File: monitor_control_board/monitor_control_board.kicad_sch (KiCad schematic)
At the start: 21 parts, among them J1 Conn_01x09_Male, J2 Conn_01x09_Male, J3 Conn_01x05_Male, J4 Conn_01x05_Male, SW1 SW_Push, SW2 SW_Push, SW3 SW_Push, SW4 SW_Push, SW5 SW_Push, SW6 SW_Push, U1 TSSP58038

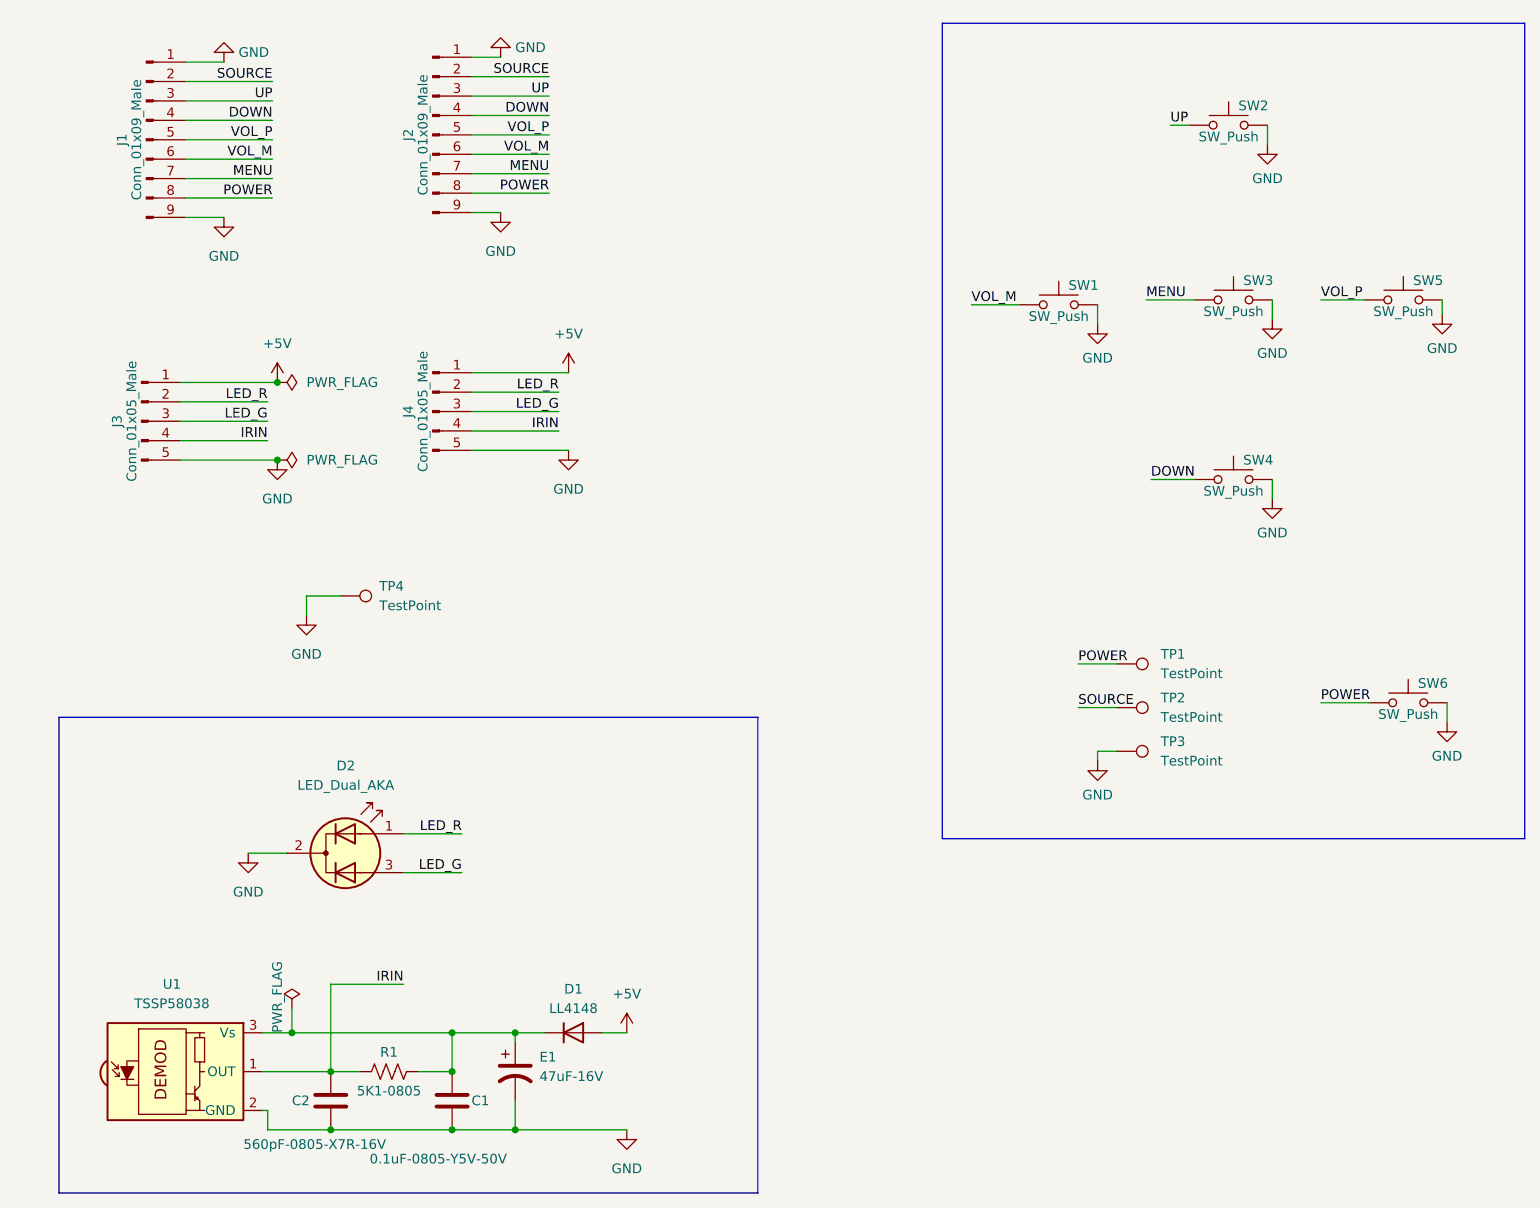
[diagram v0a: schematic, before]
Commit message: osd 컨트롤 보드 사소한 위치 조정
Signed-off-by: Ju, Gyeong-min <jcmh74@gmail.com>
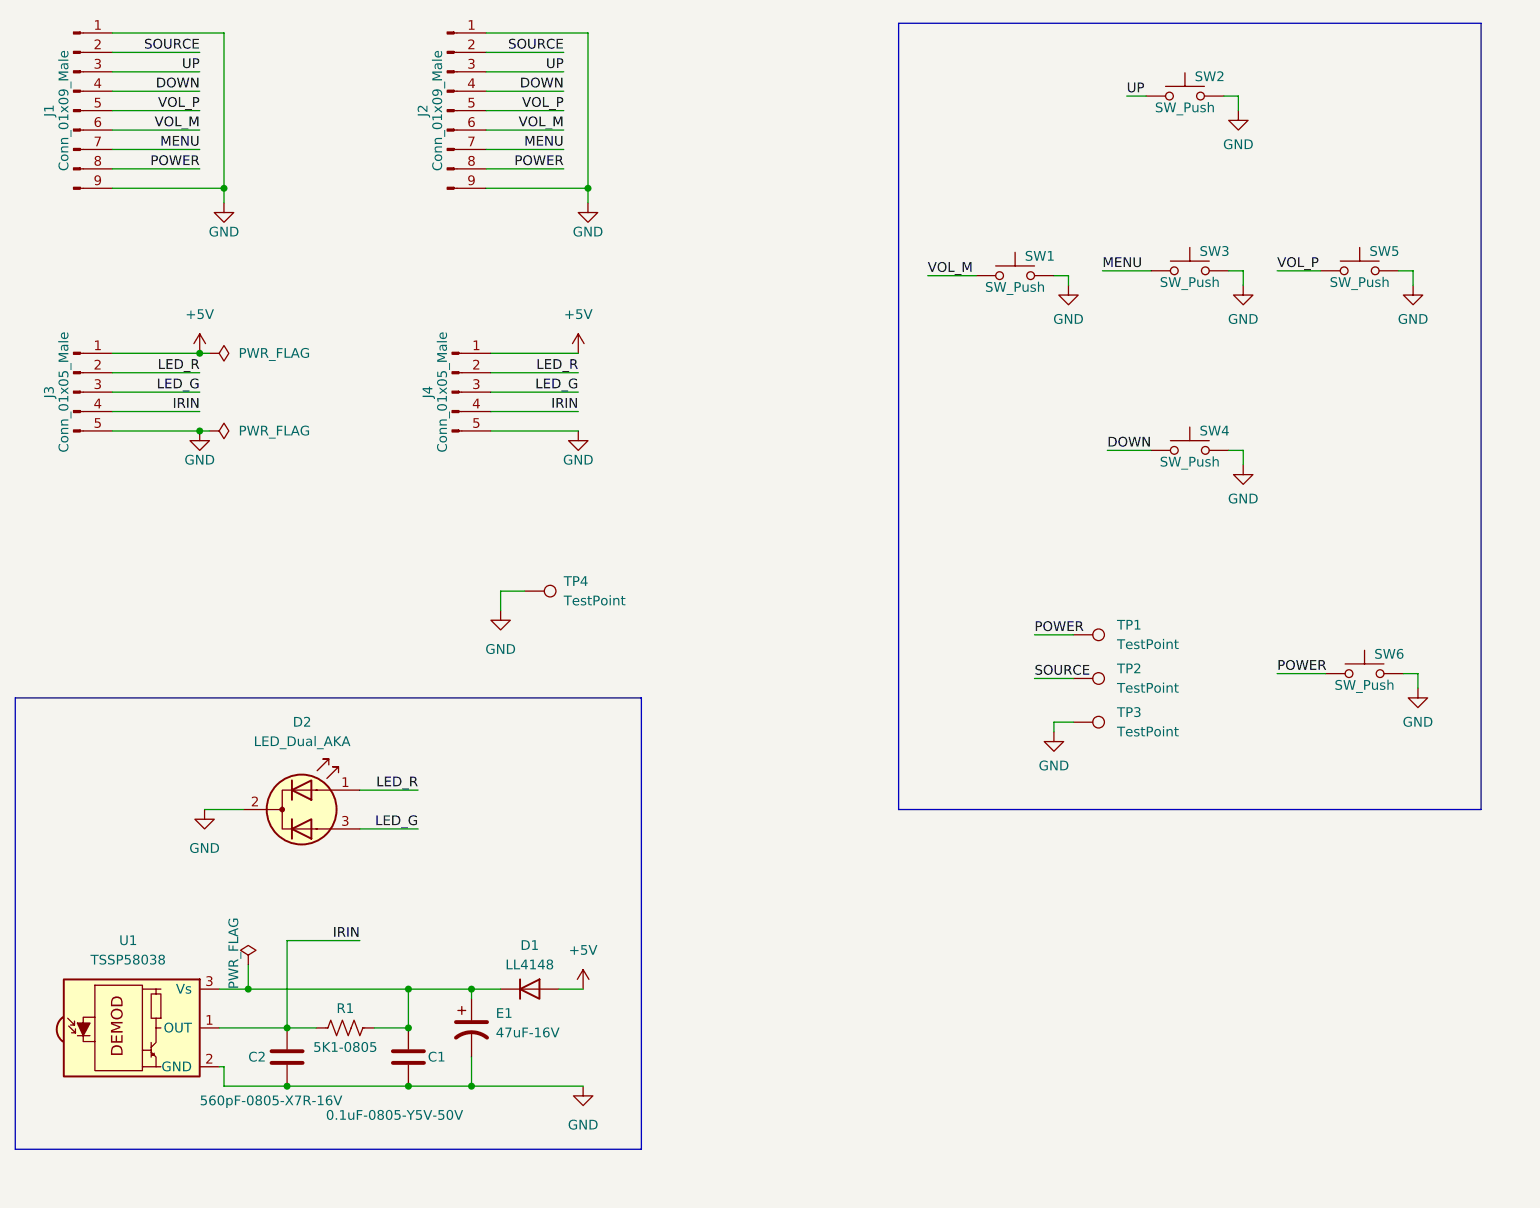
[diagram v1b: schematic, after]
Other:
- moved on the sheet: C1, C2, D1, D2, E1, J1, J2, J3, J4, R1, SW1, SW2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

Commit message: monitor_osd 배선 최적화
Signed-off-by: Ju, Gyeong-min <jcmh74@gmail.com>
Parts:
- TP1, TP2, TP3: footprint TestPoint:TestPoint_THTPad_D2.0mm_Drill1.0mm -> TestPoint:TestPoint_THTPad_D1.5mm_Drill0.7mm
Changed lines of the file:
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@@
       (effects (font (size 1.27 1.27)) (justify left))
     )
-    (property "Footprint" "TestPoint:TestPoint_THTPad_D2.0mm_Drill1.0mm" (id 2) (at 193.04 114.3 0)
+    (property "Footprint" "TestPoint:TestPoint_THTPad_D1.5mm_Drill0.7mm" (id 2) (at 193.04 114.3 0)
       (effects (font (size 1.27 1.27)) hide)
     )
@@
       (effects (font (size 1.27 1.27)) (justify left))
     )
-    (property "Footprint" "TestPoint:TestPoint_THTPad_D2.0mm_Drill1.0mm" (id 2) (at 193.04 120.015 0)
+    (property "Footprint" "TestPoint:TestPoint_THTPad_D1.5mm_Drill0.7mm" (id 2) (at 193.04 120.015 0)
       (effects (font (size 1.27 1.27)) hide)
     )
@@
       (effects (font (size 1.27 1.27)) (justify left))
     )
-    (property "Footprint" "TestPoint:TestPoint_THTPad_D2.0mm_Drill1.0mm" (id 2) (at 193.04 125.73 0)
+    (property "Footprint" "TestPoint:TestPoint_THTPad_D1.5mm_Drill0.7mm" (id 2) (at 193.04 125.73 0)
       (effects (font (size 1.27 1.27)) hide)
     )
@@
     )
     (path "/28135604-dc7c-4d8f-bee5-8abb6d80f68a"
-      (reference "TP1") (unit 1) (value "TestPoint") (footprint "TestPoint:TestPoint_THTPad_D2.0mm_Drill1.0mm")
+      (reference "TP1") (unit 1) (value "TestPoint") (footprint "TestPoint:TestPoint_THTPad_D1.5mm_Drill0.7mm")
     )
     (path "/3b934f31-2bae-48a3-8048-7da2c4d085a5"
-      (reference "TP2") (unit 1) (value "TestPoint") (footprint "TestPoint:TestPoint_THTPad_D2.0mm_Drill1.0mm")
+      (reference "TP2") (unit 1) (value "TestPoint") (footprint "TestPoint:TestPoint_THTPad_D1.5mm_Drill0.7mm")
     )
     (path "/c9f71dc3-2b4a-4ca2-8db0-36825f55689f"
-      (reference "TP3") (unit 1) (value "TestPoint") (footprint "TestPoint:TestPoint_THTPad_D2.0mm_Drill1.0mm")
+      (reference "TP3") (unit 1) (value "TestPoint") (footprint "TestPoint:TestPoint_THTPad_D1.5mm_Drill0.7mm")
     )
     (path "/a4e9f764-09ab-446a-a555-ce94ff4e73f7"

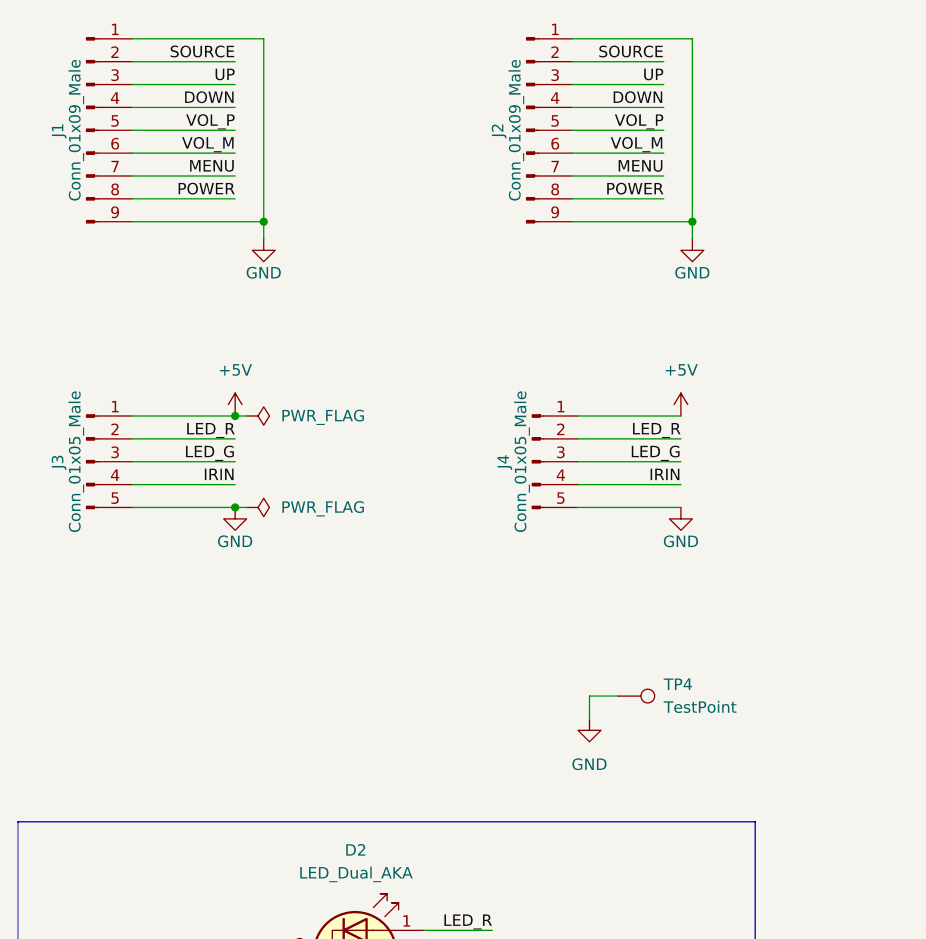
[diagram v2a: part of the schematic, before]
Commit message: monitor_osd 커넥터 모양 및 위치 변경
Signed-off-by: Ju, Gyeong-min <jcmh74@gmail.com>
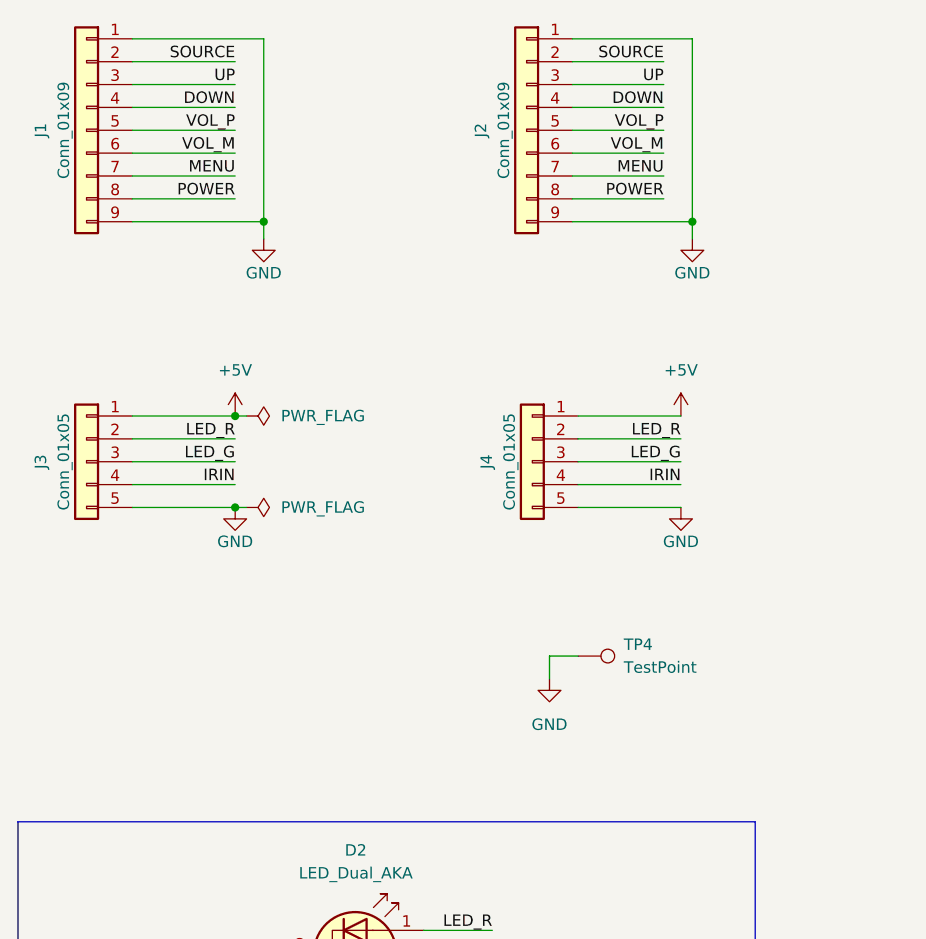
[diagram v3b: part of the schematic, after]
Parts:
- J1: value Conn_01x09_Male -> Conn_01x09; footprint Connector_JST:JST_PH_S9B-PH-K_1x09_P2.00mm_Horizontal -> Connector_PinHeader_2.00mm:PinHeader_1x09_P2.00mm_Vertical; symbol Connector:Conn_01x09_Male -> Connector_Generic:Conn_01x09
- J2: value Conn_01x09_Male -> Conn_01x09; symbol Connector:Conn_01x09_Male -> Connector_Generic:Conn_01x09
- J3: value Conn_01x05_Male -> Conn_01x05; footprint Connector_JST:JST_PH_S5B-PH-K_1x05_P2.00mm_Horizontal -> Connector_PinHeader_2.00mm:PinHeader_1x05_P2.00mm_Vertical; symbol Connector:Conn_01x05_Male -> Connector_Generic:Conn_01x05
- J4: value Conn_01x05_Male -> Conn_01x05; symbol Connector:Conn_01x05_Male -> Connector_Generic:Conn_01x05
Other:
- moved on the sheet: TP4
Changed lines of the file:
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@@
     (stroke (width 0) (type default) (color 0 0 0 0))
   )
-  (wire (pts (xy 118.11 106.045) (xy 118.11 103.505))
+  (wire (pts (xy 113.665 101.6) (xy 113.665 99.06))
     (stroke (width 0) (type default) (color 0 0 0 0))
   )
@@
     (stroke (width 0) (type default) (color 0 0 0 0))
   )
-  (wire (pts (xy 118.11 103.505) (xy 121.285 103.505))
+  (wire (pts (xy 113.665 99.06) (xy 116.84 99.06))
     (stroke (width 0) (type default) (color 0 0 0 0))
   )
@@
     (pin "1")
   )
-  (symbol (lib_id "Connector:Conn_01x05_Male") (at 111.76 77.47 0) (unit 1)
-    (in_bom yes) (on_board yes)
-    (property "Reference" "J4" (id 0) (at 108.585 77.47 90))
-    (property "Value" "Conn_01x05_Male" (id 1) (at 110.49 77.47 90))
+  (symbol (lib_id "Connector_Generic:Conn_01x05") (at 111.76 77.47 0) (mirror y) (unit 1)
+    (in_bom yes) (on_board yes)
+    (property "Reference" "J4" (id 0) (at 106.68 77.47 90))
+    (property "Value" "Conn_01x05" (id 1) (at 109.22 77.47 90))
     (property "Footprint" "Connector_PinHeader_2.54mm:PinHeader_1x05_P2.54mm_Vertical" (id 2) (at 111.76 77.47 0)
       (effects (font (size 1.27 1.27)) hide)
@@
     (pin "2")
   )
-  (symbol (lib_id "Connector:TestPoint") (at 121.285 103.505 270) (unit 1)
-    (in_bom yes) (on_board yes) (fields_autoplaced)
-    (property "Reference" "TP4" (id 0) (at 126.365 102.2349 90)
-      (effects (font (size 1.27 1.27)) (justify left))
-    )
-    (property "Value" "TestPoint" (id 1) (at 126.365 104.7749 90)
-      (effects (font (size 1.27 1.27)) (justify left))
-    )
-    (property "Footprint" "TestPoint:TestPoint_THTPad_D2.0mm_Drill1.0mm" (id 2) (at 121.285 108.585 0)
-      (effects (font (size 1.27 1.27)) hide)
-    )
-    (property "Datasheet" "~" (id 3) (at 121.285 108.585 0)
+  (symbol (lib_id "Connector:TestPoint") (at 116.84 99.06 270) (unit 1)
+    (in_bom yes) (on_board yes) (fields_autoplaced)
+    (property "Reference" "TP4" (id 0) (at 121.92 97.7899 90)
+      (effects (font (size 1.27 1.27)) (justify left))
+    )
+    (property "Value" "TestPoint" (id 1) (at 121.92 100.3299 90)
+      (effects (font (size 1.27 1.27)) (justify left))
+    )
+    (property "Footprint" "TestPoint:TestPoint_THTPad_D2.0mm_Drill1.0mm" (id 2) (at 116.84 104.14 0)
+      (effects (font (size 1.27 1.27)) hide)
+    )
+    (property "Datasheet" "~" (id 3) (at 116.84 104.14 0)
       (effects (font (size 1.27 1.27)) hide)
     )
@@
     (pin "1")
   )
-  (symbol (lib_id "Connector:Conn_01x05_Male") (at 62.23 77.47 0) (unit 1)
-    (in_bom yes) (on_board yes)
-    (property "Reference" "J3" (id 0) (at 59.055 77.47 90))
-    (property "Value" "Conn_01x05_Male" (id 1) (at 60.96 77.47 90))
-    (property "Footprint" "Connector_JST:JST_PH_S5B-PH-K_1x05_P2.00mm_Horizontal" (id 2) (at 62.23 77.47 0)
+  (symbol (lib_id "Connector_Generic:Conn_01x05") (at 62.23 77.47 0) (mirror y) (unit 1)
+    (in_bom yes) (on_board yes)
+    (property "Reference" "J3" (id 0) (at 57.15 77.47 90))
+    (property "Value" "Conn_01x05" (id 1) (at 59.69 77.47 90))
+    (property "Footprint" "Connector_PinHeader_2.00mm:PinHeader_1x05_P2.00mm_Vertical" (id 2) (at 62.23 77.47 0)
       (effects (font (size 1.27 1.27)) hide)
     )
@@
     (pin "1")
   )
-  (symbol (lib_id "Connector:Conn_01x09_Male") (at 111.125 40.64 0) (unit 1)
-    (in_bom yes) (on_board yes)
-    (property "Reference" "J2" (id 0) (at 107.95 40.64 90))
-    (property "Value" "Conn_01x09_Male" (id 1) (at 109.855 40.64 90))
+  (symbol (lib_id "Connector_Generic:Conn_01x09") (at 111.125 40.64 0) (mirror y) (unit 1)
+    (in_bom yes) (on_board yes)
+    (property "Reference" "J2" (id 0) (at 106.045 40.64 90))
+    (property "Value" "Conn_01x09" (id 1) (at 108.585 40.64 90))
     (property "Footprint" "Connector_PinHeader_2.54mm:PinHeader_1x09_P2.54mm_Vertical" (id 2) (at 111.125 40.64 0)
       (effects (font (size 1.27 1.27)) hide)
@@
     (pin "1")
   )
-  (symbol (lib_id "Connector:Conn_01x09_Male") (at 62.23 40.64 0) (unit 1)
-    (in_bom yes) (on_board yes)
-    (property "Reference" "J1" (id 0) (at 59.055 40.64 90))
-    (property "Value" "Conn_01x09_Male" (id 1) (at 60.96 40.64 90))
-    (property "Footprint" "Connector_JST:JST_PH_S9B-PH-K_1x09_P2.00mm_Horizontal" (id 2) (at 62.23 40.64 0)
+  (symbol (lib_id "Connector_Generic:Conn_01x09") (at 62.23 40.64 0) (mirror y) (unit 1)
+    (in_bom yes) (on_board yes)
+    (property "Reference" "J1" (id 0) (at 57.15 40.64 90))
+    (property "Value" "Conn_01x09" (id 1) (at 59.69 40.64 90))
+    (property "Footprint" "Connector_PinHeader_2.00mm:PinHeader_1x09_P2.00mm_Vertical" (id 2) (at 62.23 40.64 0)
       (effects (font (size 1.27 1.27)) hide)
     )
@@
     (pin "1")
   )
-  (symbol (lib_id "power:GND") (at 118.11 106.045 0) (unit 1)
-    (in_bom yes) (on_board yes) (fields_autoplaced)
-    (property "Reference" "#PWR0118" (id 0) (at 118.11 112.395 0)
-      (effects (font (size 1.27 1.27)) hide)
-    )
-    (property "Value" "GND" (id 1) (at 118.11 111.125 0))
-    (property "Footprint" "" (id 2) (at 118.11 106.045 0)
-      (effects (font (size 1.27 1.27)) hide)
-    )
-    (property "Datasheet" "" (id 3) (at 118.11 106.045 0)
+  (symbol (lib_id "power:GND") (at 113.665 101.6 0) (unit 1)
+    (in_bom yes) (on_board yes) (fields_autoplaced)
+    (property "Reference" "#PWR0118" (id 0) (at 113.665 107.95 0)
+      (effects (font (size 1.27 1.27)) hide)
+    )
+    (property "Value" "GND" (id 1) (at 113.665 106.68 0))
+    (property "Footprint" "" (id 2) (at 113.665 101.6 0)
+      (effects (font (size 1.27 1.27)) hide)
+    )
+    (property "Datasheet" "" (id 3) (at 113.665 101.6 0)
       (effects (font (size 1.27 1.27)) hide)
     )
@@
     )
     (path "/d3c266d1-a6ac-4741-aed1-d763f0d10aee"
-      (reference "J1") (unit 1) (value "Conn_01x09_Male") (footprint "Connector_JST:JST_PH_S9B-PH-K_1x09_P2.00mm_Horizontal")
+      (reference "J1") (unit 1) (value "Conn_01x09") (footprint "Connector_PinHeader_2.00mm:PinHeader_1x09_P2.00mm_Vertical")
     )
     (path "/bd6046eb-2439-4157-89c1-25727144afe1"
-      (reference "J2") (unit 1) (value "Conn_01x09_Male") (footprint "Connector_PinHeader_2.54mm:PinHeader_1x09_P2.54mm_Vertical")
+      (reference "J2") (unit 1) (value "Conn_01x09") (footprint "Connector_PinHeader_2.54mm:PinHeader_1x09_P2.54mm_Vertical")
     )
     (path "/b4401dcf-782e-4b57-8c6d-34c2256178fa"
-      (reference "J3") (unit 1) (value "Conn_01x05_Male") (footprint "Connector_JST:JST_PH_S5B-PH-K_1x05_P2.00mm_Horizontal")
+      (reference "J3") (unit 1) (value "Conn_01x05") (footprint "Connector_PinHeader_2.00mm:PinHeader_1x05_P2.00mm_Vertical")
     )
     (path "/45fa85cf-e83e-46d2-ae9e-e1723a23a31c"
-      (reference "J4") (unit 1) (value "Conn_01x05_Male") (footprint "Connector_PinHeader_2.54mm:PinHeader_1x05_P2.54mm_Vertical")
+      (reference "J4") (unit 1) (value "Conn_01x05") (footprint "Connector_PinHeader_2.54mm:PinHeader_1x05_P2.54mm_Vertical")
     )
     (path "/2d726375-5dfe-47ee-ad24-a1e19b589c54"
